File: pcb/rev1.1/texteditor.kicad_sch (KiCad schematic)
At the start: 18 parts, among them J1 Conn_02x08_Odd_Even, J2 SD_Module, J3 Power In (7v-20v), J4 LED, J5 Contrast Breakout, J6 LED Potentiometer, J7 Conn_01x03, J8 Conn_01x03, J9 Contrast Potentiometer, Q1 BC547, SW1 SW_SPDT, U2 L7805

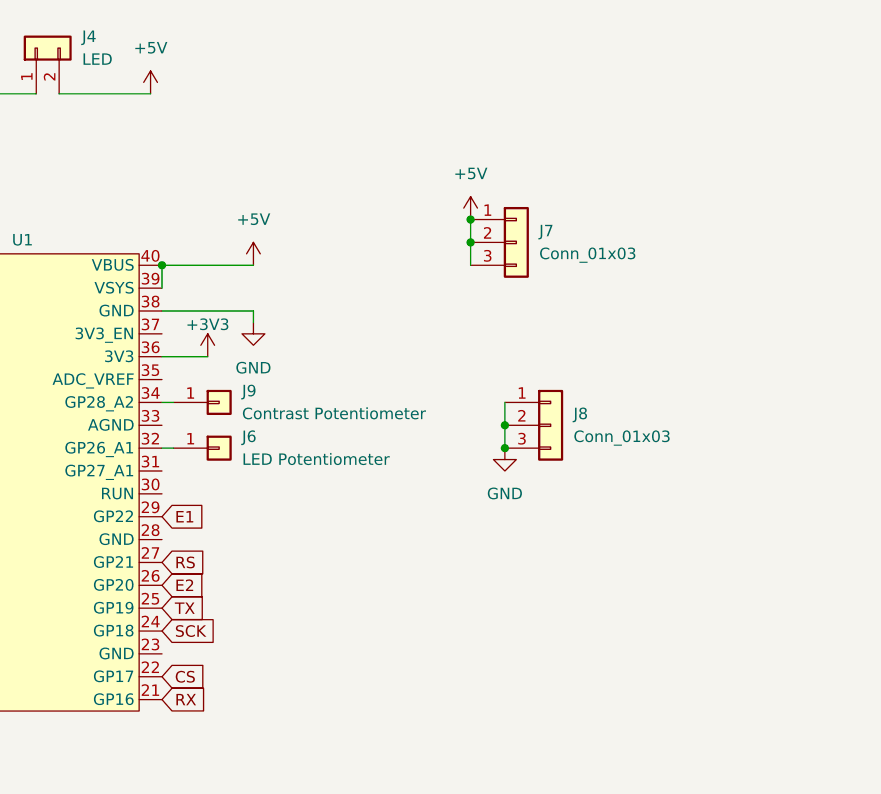
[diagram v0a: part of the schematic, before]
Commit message: Add better headers for potentiometers
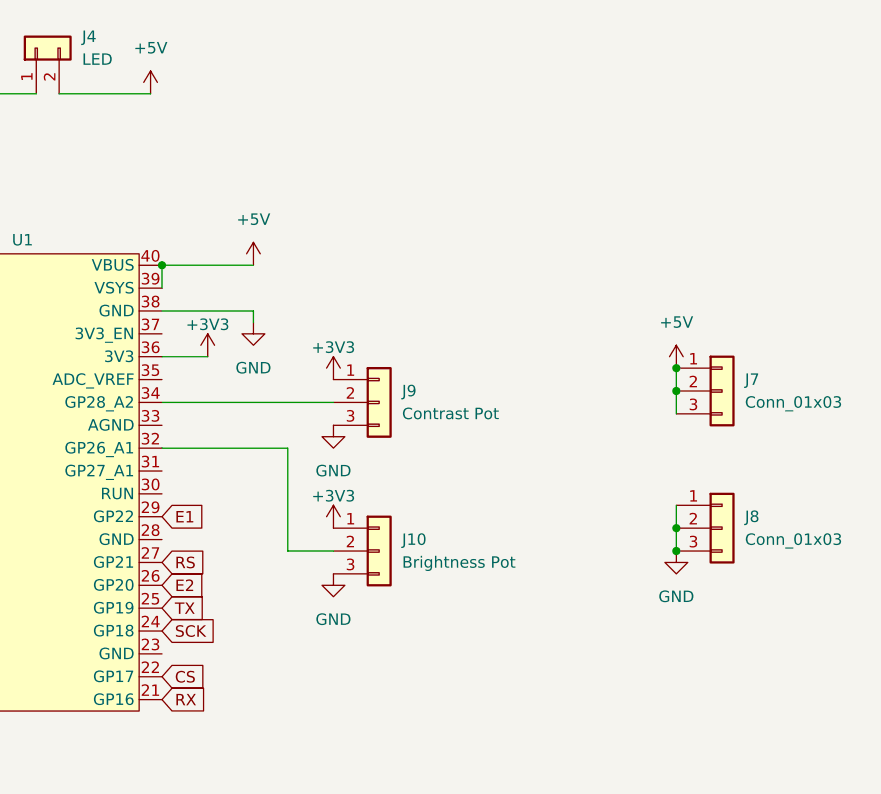
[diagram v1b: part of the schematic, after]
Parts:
- removed J6: LED Potentiometer, Connector_PinHeader_2.54mm:PinHeader_1x01_P2.54mm_Vertical, symbol Connector_Generic:Conn_01x01
- removed J9: Contrast Potentiometer, Connector_PinHeader_2.54mm:PinHeader_1x01_P2.54mm_Vertical, symbol Connector_Generic:Conn_01x01
- added J10: Brightness Pot, Connector_PinHeader_2.54mm:PinHeader_1x03_P2.54mm_Vertical, symbol Connector_Generic:Conn_01x03
- added J9: Contrast Pot, Connector_PinHeader_2.54mm:PinHeader_1x03_P2.54mm_Vertical, symbol Connector_Generic:Conn_01x03
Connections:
- net +3V3: now also J10.1 (Pin_1), J9.1 (Pin_1)
- net GND: now also J10.3 (Pin_3), J9.3 (Pin_3)
- net at U1.32 (GP26_A1): now also J10.2 (Pin_2)
- net at U1.34 (GP28_A2): now also J9.2 (Pin_2)
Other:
- moved on the sheet: J7, J8
